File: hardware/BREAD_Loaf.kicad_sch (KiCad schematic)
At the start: 27 parts, among them J1 PPPC101LGBN-RC, J2 THING_PLUS_LOGICAL, Q1 BSS138, Q2 BSS138, Q3 BSS138, U1 AP63205WU-7, U2 LTC4311ISC6-TRMPBF

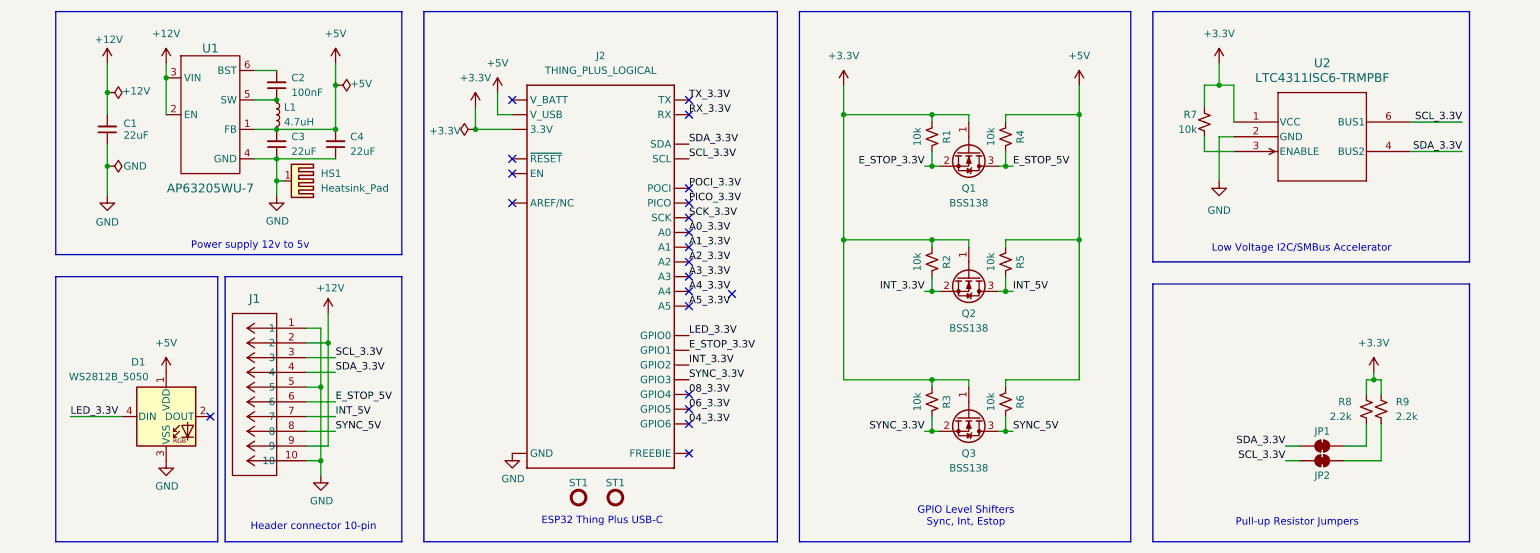
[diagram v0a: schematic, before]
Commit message: fix(hw): re-point remaining library references
Every symbol now resolves against KiCad-Master-Lib:

  LTC4311:LTC4311ISC6-TRMPBF        -> KMLib_IC_Digital:LTC4311ISC6-TRMPBF
  SparkFun-RF:ESP_THING_PLUS_LOGICAL -> SparkFun-Board:ThingPlus_With_Connectors
  SparkFun-Hardware:Stand_off, PPPC101LGBN-RC, Arc  -> resolved

Board is clean: validate_board PASS, 0 ERC errors, 0 DRC errors.
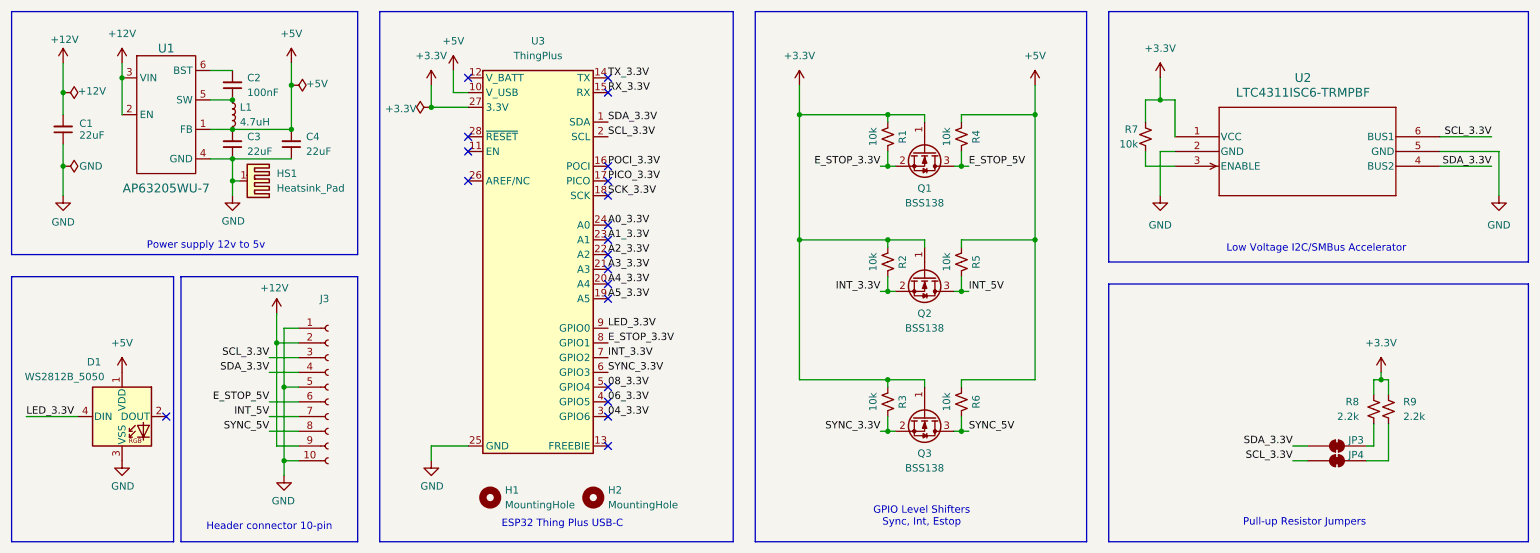
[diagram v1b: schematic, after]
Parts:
- removed J1: PPPC101LGBN-RC, Connector_PinSocket_2.54mm:PinSocket_1x10_P2.54mm_Horizontal, symbol PPPC101LGBN-RC:PPPC101LGBN-RC
- removed J2: THING_PLUS_LOGICAL, SparkFun-Board:ThingPlus, symbol SparkFun-RF:ESP_THING_PLUS_LOGICAL
- removed JP1, JP2: (no value), SparkFun-Jumper:Jumper_2_NC_Trace, symbol SparkFun-Jumper:SolderJumper_2_Bridged
- removed ST1 (x2): Stand_off, SparkFun-Hardware:Standoff, symbol SparkFun-Hardware:Stand_off
- added H1, H2: MountingHole, MountingHole:MountingHole_3.2mm_M3, symbol Mechanical:MountingHole
- added J3: Conn_01x10_Socket, Connector_PinSocket_2.54mm:PinSocket_1x10_P2.54mm_Horizontal, symbol Connector:Conn_01x10_Socket
- added JP3, JP4: SolderJumper_2_Bridged, Jumper:SolderJumper-2_P1.3mm_Bridged_Pad1.0x1.5mm, symbol Jumper:SolderJumper_2_Bridged
- added U3: ThingPlus, SparkFun-Board:ThingPlus_With_Connectors, symbol SparkFun-Board:ThingPlus_With_Connectors
- D1: symbol SparkFun-LED:WS2812B_5050 -> KMLib_IC_Digital:WS2812B_5050_RGB_LED; PROD_ID (none) -> DIO-12503
- U1: footprint Package_TO_SOT_SMD:TSOT-23-6 -> KMLib_IC_SMD:SOIC_05WU-7_DIO
- U2: footprint Package_TO_SOT_SMD:SOT-363_SC-70-6 -> KMLib_IC_SMD:SOT-6_SC_LIT; symbol LTC4311:LTC4311ISC6-TRMPBF -> KMLib_IC_Digital:LTC4311ISC6-TRMPBF
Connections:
- net +12V: now also J3.2 (Pin_2), J3.9 (Pin_9)
- net +3.3V: now also U3.27 (3.3V)
- net +5V: now also U3.10 (V_USB)
- net 04_3.3V: now also U3.3 (GPIO6)
- net 06_3.3V: now also U3.4 (GPIO5)
- net 08_3.3V: now also U3.5 (GPIO4)
- net A0_3.3V: now also U3.24 (A0)
- net A1_3.3V: now also U3.23 (A1)
- net A2_3.3V: now also U3.22 (A2)
- net A3_3.3V: now also U3.21 (A3)
- net A4_3.3V: now also U3.20 (A4)
- net A5_3.3V: now also U3.19 (A5)
- net E_STOP_3.3V: now also U3.8 (GPIO1)
- net E_STOP_5V: now also J3.6 (Pin_6)
- net GND: now also J3.1 (Pin_1), J3.10 (Pin_10), J3.5 (Pin_5), U3.25 (GND)
- net INT_3.3V: now also U3.7 (GPIO2)
- net INT_5V: now also J3.7 (Pin_7)
- net LED_3.3V: now also U3.9 (GPIO0)
- net PICO_3.3V: now also U3.17 (PICO)
- net POCI_3.3V: now also U3.16 (POCI)
- net RX_3.3V: now also U3.15 (RX)
- net SCK_3.3V: now also U3.18 (SCK)
- net SCL_3.3V: now also J3.3 (Pin_3), JP4.1 (A), U3.2 (SCL)
- net SDA_3.3V: now also J3.4 (Pin_4), JP3.1 (A), U3.1 (SDA)
- net SYNC_3.3V: now also U3.6 (GPIO3)
- net SYNC_5V: now also J3.8 (Pin_8)
- net TX_3.3V: now also U3.14 (TX)
- net at R9.2: now also JP4.2 (B)
- net at R8.2: now also JP3.2 (B)
- no-connect marks 21 -> 20
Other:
- moved on the sheet: C1, C2, C3, C4, D1, HS1, L1, Q1, Q2, Q3, R1, R2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
